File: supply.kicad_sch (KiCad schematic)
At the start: 75 parts, among them J3 Molex_Nano-Fit_1x2_SMD_105430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, Q4 BCM857BS-7-F, Q5 BCM857BS-7-F

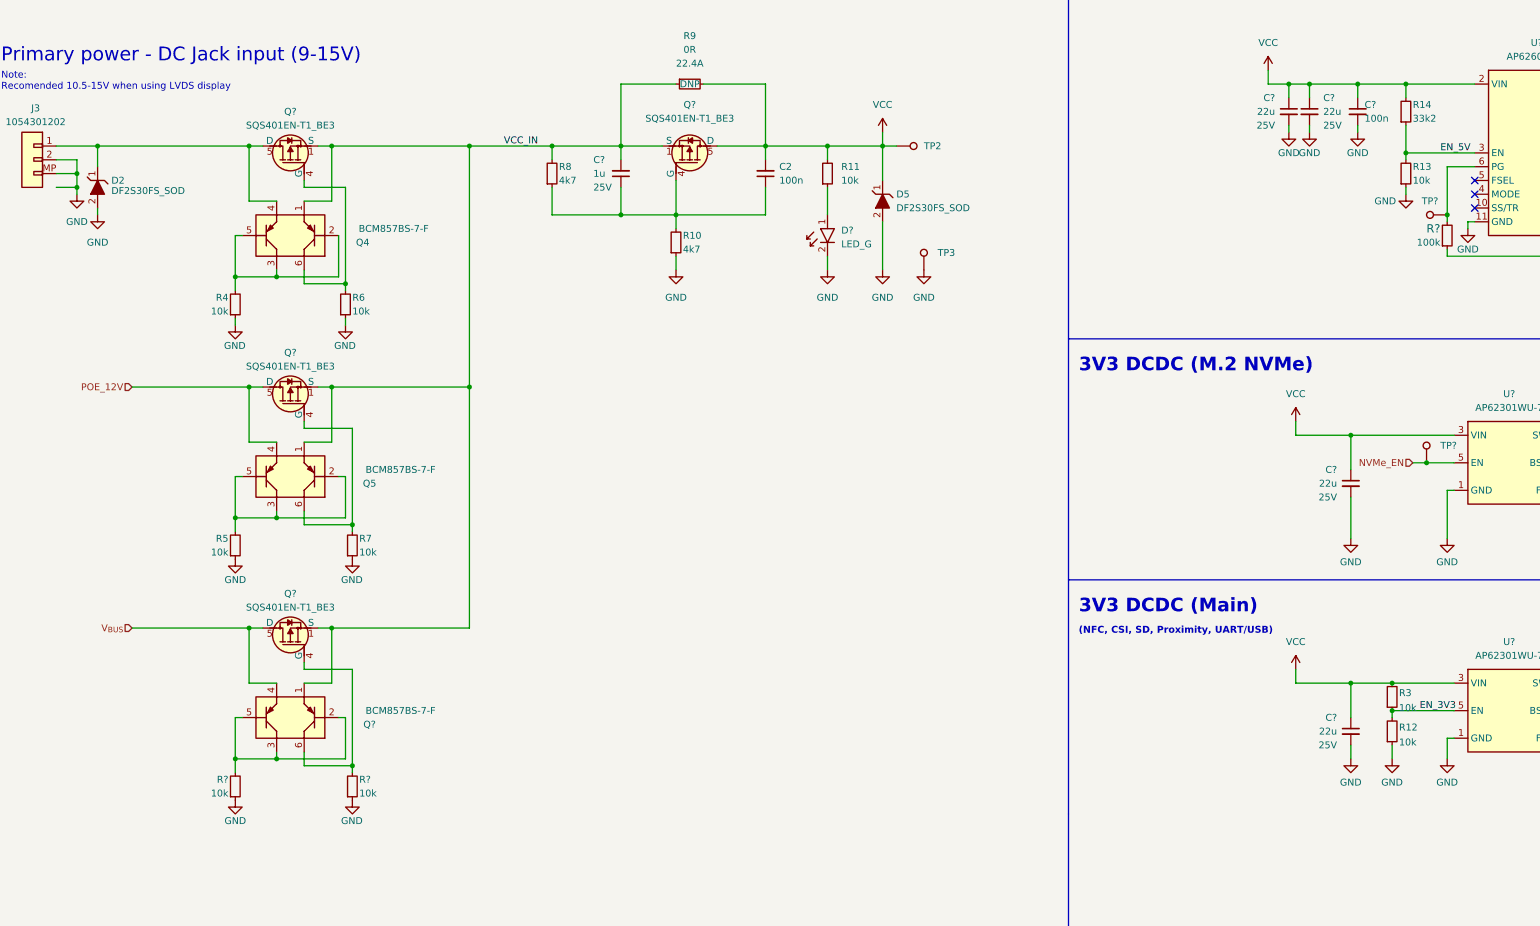
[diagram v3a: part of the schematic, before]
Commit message: [#54617] Review requested: Change ideal diode controller
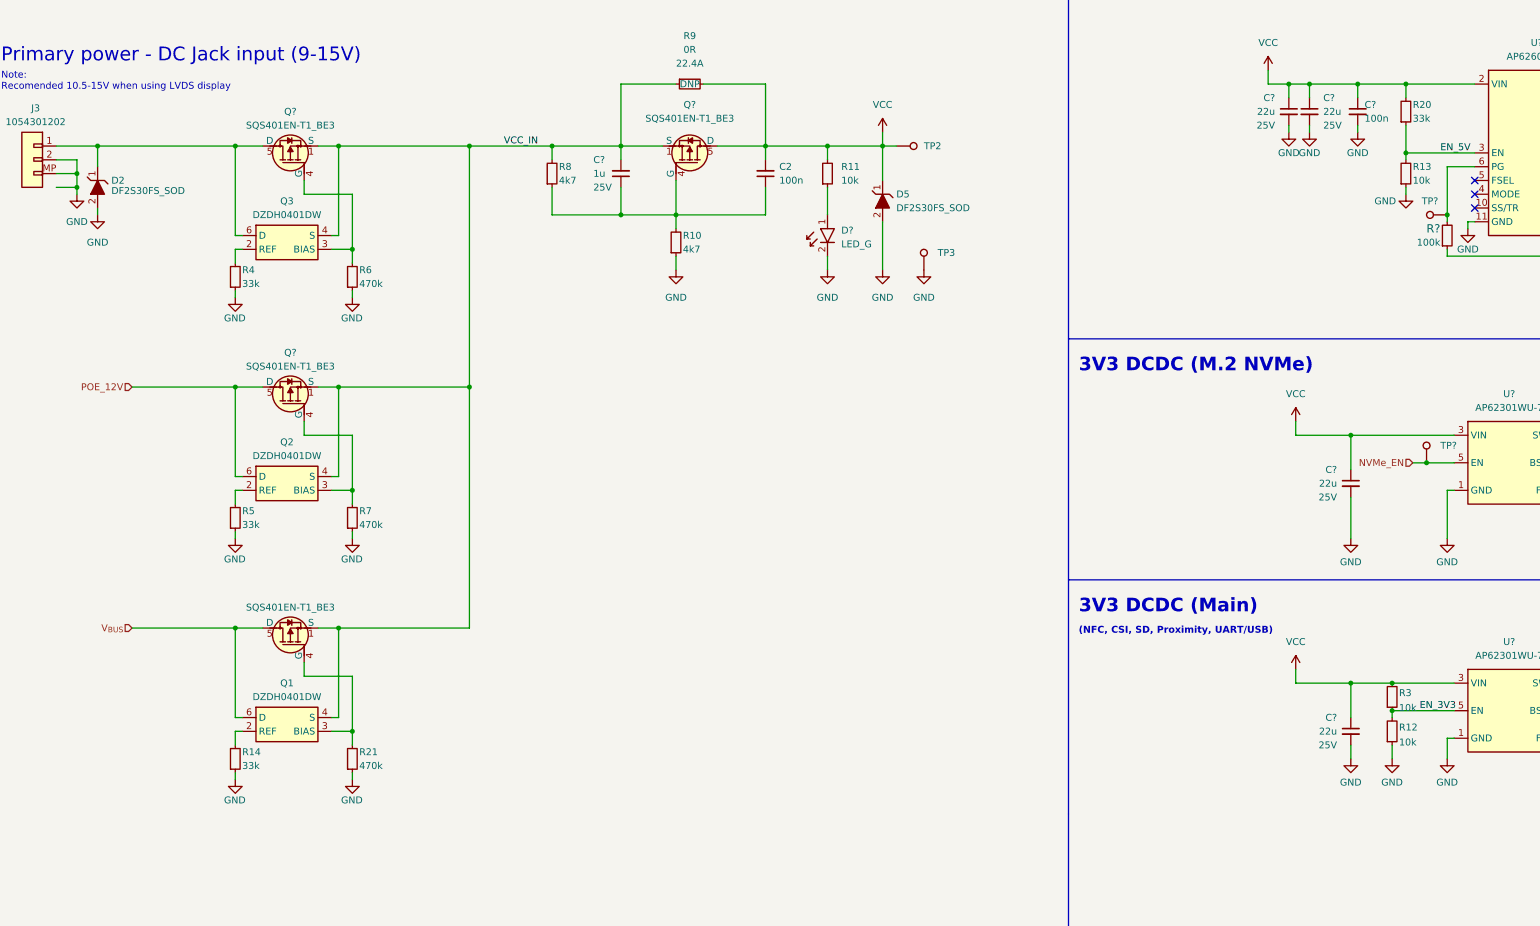
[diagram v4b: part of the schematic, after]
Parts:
- removed Q4, Q5, Q?: BCM857BS-7-F, antmicro-footprints:SOT-363, symbol antmicroTransistorsBipolarArrays:BCM857BS-7-F
- removed R14: R_33k2_0402, antmicro-footprints:R_0402_1005Metric, symbol antmicroResistors0402:R_33k2_0402
- removed R4, R5, R6, R7, R? (x2): R_10k_0402, antmicro-footprints:R_0402_1005Metric, symbol antmicroResistors0402:R_10k_0402
- added Q1, Q2, Q3: DZDH0401DW, antmicro-footprints:SOT-363, symbol antmicroPMICORControllersIdealDiodes:DZDH0401DW
- added R14, R20, R4, R5: R_33k_0402, antmicro-footprints:R_0402_1005Metric, symbol antmicroResistors0402:R_33k_0402
- added R21, R6, R7: R_470k_0402, antmicro-footprints:R_0402_1005Metric, symbol antmicroResistors0402:R_470k_0402
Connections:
- net EN_5V: now also R20.1
- net GND: now also R14.1, R21.1, R4.1, R5.1, R6.1, R7.1
- net POE_12V: now also Q2.6 (D)
- net VCC: now also R20.2
- net VCC_IN: now also Q1.4 (S), Q2.4 (S), Q3.4 (S)
- net V_{BUS}: now also Q1.6 (D)
- net at Q?.4 (G): now also Q3.3 (BIAS), R6.2
- net at Q?.4 (G): now also Q2.3 (BIAS), R7.2
- net at D2.1, J3.1, Q?.5 (D): now also Q3.6 (D)
- net at Q?.4 (G): now also Q1.3 (BIAS), R21.2
- new net: Q3.2 (REF), R4.2
- new net: Q1.2 (REF), R14.2
- new net: Q2.2 (REF), R5.2

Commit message: [#54617] Review requested changes
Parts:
- R9, R? (x3): Tolerance (none) -> template_tolerance

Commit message: [#54617] Re-enumerate reference designators
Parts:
- removed TP? (x3): TP_0.75mm_SMD, antmicro-footprints:TP_SMD_0.75mm, symbol antmicroTestPoints:TP_0.75mm_SMD
- gave numbers to parts that had none: 44
- renumbered C2 to C302, D2 to D301, D5 to D303, J3 to J301, Q3 to Q301, Q2 to Q302, Q1 to Q303, R4 to R301, R5 to R302, R14 to R303, R6 to R304, R7 to R305, R21 to R306, R8 to R307, R9 to R308, R10 to R309, R11 to R310, R3 to R311, R12 to R312, R20 to R313, R13 to R314, R19 to R317, R17 to R318, R18 to R319, R16 to R320, R15 to R321, TP2 to TP301, TP3 to TP302
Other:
- moved on the sheet: C306, C312, C315, C318, L303, R311, R312, R316, R317, R324

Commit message: [#55181] Rotate board; Change CSI&SD position; Update adapter; NFC placement
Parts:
- TP303, TP304: footprint antmicro-footprints:TP_SMD_1mm -> antmicro-footprints:TP_SMD_0.75mm; symbol antmicroTestPoints:TP_1mm_SMD -> antmicroTestPoints:TP_0.75mm_SMD; now left out of the parts list
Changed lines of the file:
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@@
     )
   )
-  (symbol (lib_id "antmicroTestPoints:TP_1mm_SMD") (at 285.75 180.34 90) (unit 1)
-    (in_bom yes) (on_board yes) (dnp no)
+  (symbol (lib_id "antmicroTestPoints:TP_0.75mm_SMD") (at 285.75 180.34 90) (unit 1)
+    (in_bom no) (on_board yes) (dnp no)
     (property "Reference" "TP303" (at 278.13 177.8 90)
       (effects (font (size 1.27 1.27) (thickness 0.15)) (justify right))
@@
       (effects (font (size 1.27 1.27) (thickness 0.15)) (justify left bottom) hide)
     )
-    (property "Footprint" "antmicro-footprints:TP_SMD_1mm" (at 295.91 165.1 0)
-      (effects (font (size 1.27 1.27) (thickness 0.15)) (justify left bottom) hide)
-    )
-    (property "Datasheet" "" (at 298.45 165.1 0)
-      (effects (font (size 1.27 1.27) (thickness 0.15)) (justify left bottom) hide)
-    )
-    (property "Author" "Antmicro" (at 300.99 165.1 0)
-      (effects (font (size 1.27 1.27) (thickness 0.15)) (justify left bottom) hide)
-    )
-    (property "License" "Apache-2.0" (at 303.53 165.1 0)
-      (effects (font (size 1.27 1.27) (thickness 0.15)) (justify left bottom) hide)
-    )
-    (property "MPN" "" (at 285.75 180.34 0)
-      (effects (font (size 1.27 1.27)) hide)
-    )
-    (property "Manufacturer" "" (at 285.75 180.34 0)
-      (effects (font (size 1.27 1.27)) hide)
+    (property "Footprint" "antmicro-footprints:TP_SMD_0.75mm" (at 292.1 169.545 0)
+      (effects (font (size 1.27 1.27) (thickness 0.15)) (justify left bottom) hide)
+    )
+    (property "Datasheet" "" (at 298.45 162.56 0)
+      (effects (font (size 1.27 1.27) (thickness 0.15)) (justify left bottom) hide)
+    )
+    (property "Author" "Antmicro" (at 294.64 169.545 0)
+      (effects (font (size 1.27 1.27) (thickness 0.15)) (justify left bottom) hide)
+    )
+    (property "License" "Apache-2.0" (at 297.18 169.545 0)
+      (effects (font (size 1.27 1.27) (thickness 0.15)) (justify left bottom) hide)
+    )
+    (property "MPN" "" (at 297.18 169.545 0)
+      (effects (font (size 1.27 1.27) (thickness 0.15)) (justify left bottom) hide)
+    )
+    (property "Manufacturer" "" (at 292.1 169.545 0)
+      (effects (font (size 1.27 1.27) (thickness 0.15)) (justify left bottom) hide)
     )
     (pin "1")
@@
     )
   )
-  (symbol (lib_id "antmicroTestPoints:TP_1mm_SMD") (at 289.56 134.62 0) (mirror y) (unit 1)
-    (in_bom yes) (on_board yes) (dnp no) (fields_autoplaced)
+  (symbol (lib_id "antmicroTestPoints:TP_0.75mm_SMD") (at 289.56 134.62 0) (mirror y) (unit 1)
+    (in_bom no) (on_board yes) (dnp no) (fields_autoplaced)
     (property "Reference" "TP304" (at 286.385 132.08 0)
       (effects (font (size 1.27 1.27) (thickness 0.15)))
@@
       (effects (font (size 1.27 1.27) (thickness 0.15)) (justify left bottom) hide)
     )
-    (property "Footprint" "antmicro-footprints:TP_SMD_1mm" (at 274.32 144.78 0)
-      (effects (font (size 1.27 1.27) (thickness 0.15)) (justify left bottom) hide)
-    )
-    (property "Datasheet" "" (at 274.32 147.32 0)
-      (effects (font (size 1.27 1.27) (thickness 0.15)) (justify left bottom) hide)
-    )
-    (property "Author" "Antmicro" (at 274.32 149.86 0)
-      (effects (font (size 1.27 1.27) (thickness 0.15)) (justify left bottom) hide)
-    )
-    (property "License" "Apache-2.0" (at 274.32 152.4 0)
-      (effects (font (size 1.27 1.27) (thickness 0.15)) (justify left bottom) hide)
-    )
-    (property "MPN" "" (at 289.56 134.62 0)
-      (effects (font (size 1.27 1.27)) hide)
-    )
-    (property "Manufacturer" "" (at 289.56 134.62 0)
-      (effects (font (size 1.27 1.27)) hide)
-    )
-    (pin "1")
+    (property "Footprint" "antmicro-footprints:TP_SMD_0.75mm" (at 278.765 140.97 0)
+      (effects (font (size 1.27 1.27) (thickness 0.15)) (justify left bottom) hide)
+    )
+    (property "Datasheet" "" (at 271.78 147.32 0)
+      (effects (font (size 1.27 1.27) (thickness 0.15)) (justify left bottom) hide)
+    )
+    (property "Author" "Antmicro" (at 278.765 143.51 0)
+      (effects (font (size 1.27 1.27) (thickness 0.15)) (justify left bottom) hide)
+    )
+    (property "License" "Apache-2.0" (at 278.765 146.05 0)
+      (effects (font (size 1.27 1.27) (thickness 0.15)) (justify left bottom) hide)
+    )
+    (property "MPN" "" (at 278.765 146.05 0)
+      (effects (font (size 1.27 1.27) (thickness 0.15)) (justify left bottom) hide)
+    )
+    (property "Manufacturer" "" (at 278.765 140.97 0)
+      (effects (font (size 1.27 1.27) (thickness 0.15)) (justify left bottom) hide)
+    )
+    (pin "1")

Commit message: [#55181] PCB: PoE: Placement
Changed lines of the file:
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@@
   (junction (at 345.44 110.49) (diameter 0) (color 0 0 0 0)
-  )
-  (junction (at 36.83 129.54) (diameter 0) (color 0 0 0 0)
   )
   (junction (at 355.6 220.98) (diameter 0) (color 0 0 0 0)
@@
     (stroke (width 0) (type default))
   )
-  (wire (pts (xy 36.83 129.54) (xy 36.83 130.81))
-    (stroke (width 0) (type default))
-  )
   (wire (pts (xy 334.01 182.88) (xy 334.01 185.42))
     (stroke (width 0) (type default))
@@
     (stroke (width 0) (type default))
   )
-  (wire (pts (xy 33.02 129.54) (xy 36.83 129.54))
-    (stroke (width 0) (type default))
-  )
   (wire (pts (xy 33.02 124.46) (xy 36.83 124.46))
     (stroke (width 0) (type default))
@@
     (stroke (width 0) (type default))
   )
-  (wire (pts (xy 36.83 127) (xy 36.83 129.54))
-    (stroke (width 0) (type default))
-  )
+  (wire (pts (xy 36.83 127) (xy 36.83 130.81))
+    (stroke (width 0) (type default))
+  )
